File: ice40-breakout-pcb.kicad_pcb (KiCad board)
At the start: 2 copper layers, 56 x 78.3 mm, 59 parts, among them J1 USB_B_Micro, J2 USB_Break_Out, J3 Conn_02x16_Odd_Even, J4 Conn_02x16_Odd_Even, J5 Conn_02x16_Odd_Even, J6 Conn_02x04_Odd_Even, U1 SIT2001BI-S2-33E-12.000000G, U2 TLV73333PDBV, U3 TLV73312PDBV, U4 AT25SF081-SHD-X, U5 ICE40HX4K-TQ144

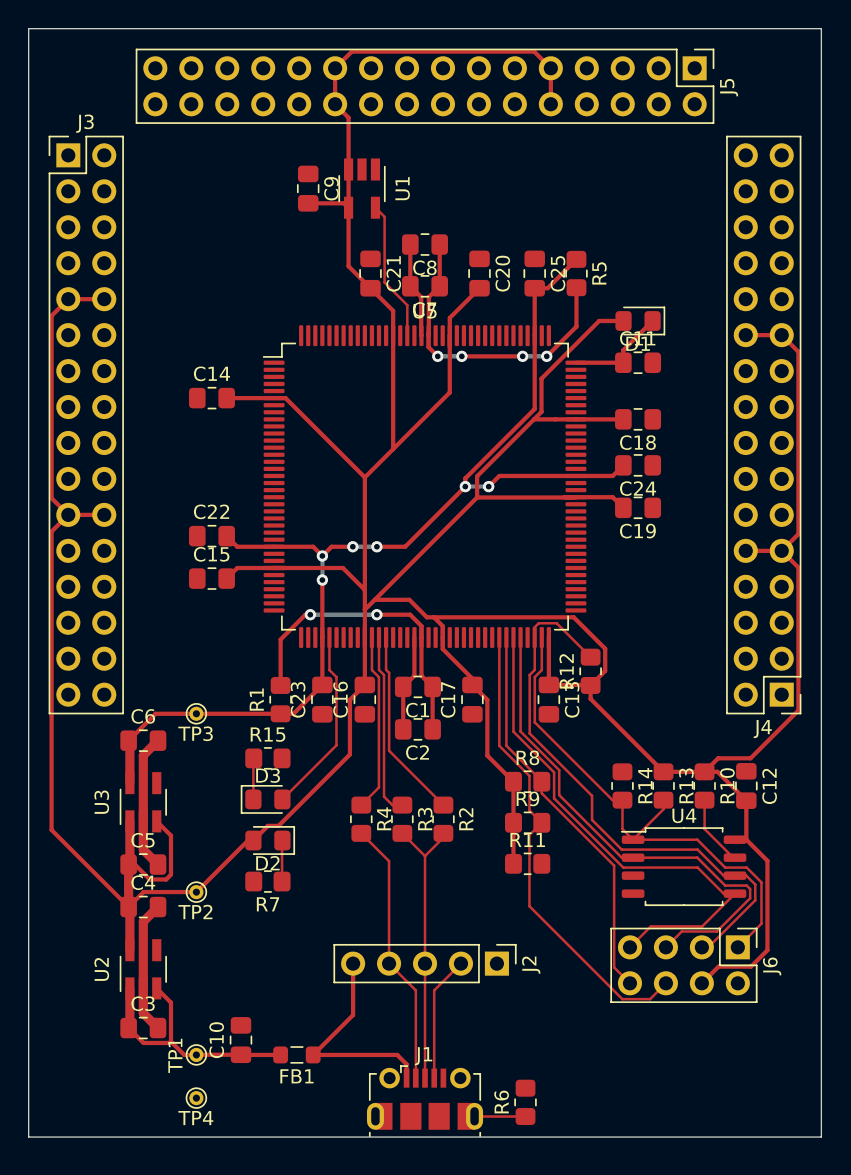
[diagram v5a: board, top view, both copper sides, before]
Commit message: Initial routing of GPIO.
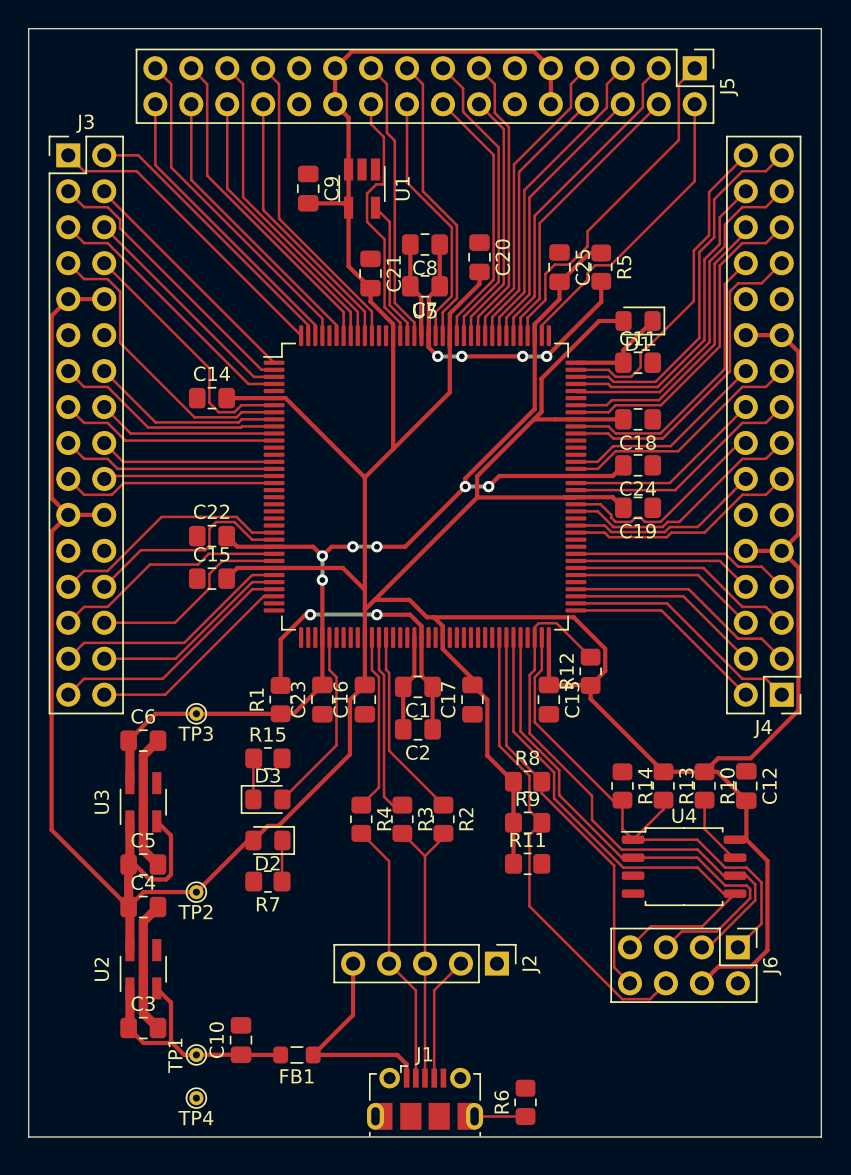
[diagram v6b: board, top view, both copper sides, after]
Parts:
- moved C25 1.81 mm to (129.5, 74.5)
- moved R5 1.81 mm to (132.4, 74.5)
- moved C20 1.15 mm to (123.8, 73.8)
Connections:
- J3 pad 1: Net-(J3-Pad1) -> gp_a_1
- J3 pad 13: Net-(J3-Pad13) -> gp_a_9
- J3 pad 14: Net-(J3-Pad14) -> gp_a_10
- J3 pad 15: Net-(J3-Pad15) -> gp_a_11
- J3 pad 16: Net-(J3-Pad16) -> gp_a_12
- J3 pad 17: Net-(J3-Pad17) -> gp_a_13
- J3 pad 18: Net-(J3-Pad18) -> gp_a_14
- J3 pad 19: Net-(J3-Pad19) -> gp_a_15
- J3 pad 2: Net-(J3-Pad2) -> gp_a_2
- J3 pad 20: Net-(J3-Pad20) -> gp_a_16
- J3 pad 25: Net-(J3-Pad25) -> gp_a_17
- J3 pad 26: Net-(J3-Pad26) -> gp_a_18
- J3 pad 27: Net-(J3-Pad27) -> gp_a_19
- J3 pad 28: Net-(J3-Pad28) -> gp_a_20
- J3 pad 29: Net-(J3-Pad29) -> gp_a_21
- J3 pad 3: Net-(J3-Pad3) -> gp_a_3
- J3 pad 30: Net-(J3-Pad30) -> gp_a_22
- J3 pad 31: Net-(J3-Pad31) -> gp_a_23
- J3 pad 32: Net-(J3-Pad32) -> gp_a_24
- J3 pad 4: Net-(J3-Pad4) -> gp_a_4
- J3 pad 5: Net-(J3-Pad5) -> gp_a_5
- J3 pad 6: Net-(J3-Pad6) -> gp_a_6
- J3 pad 7: Net-(J3-Pad7) -> gp_a_7
- J3 pad 8: Net-(J3-Pad8) -> gp_a_8
- J4 pad 1: Net-(J4-Pad1) -> gp_c_1
- J4 pad 13: Net-(J4-Pad13) -> gp_c_9
- J4 pad 14: Net-(J4-Pad14) -> gp_c_10
- J4 pad 15: Net-(J4-Pad15) -> gp_c_11
- J4 pad 16: Net-(J4-Pad16) -> gp_c_12
- J4 pad 17: Net-(J4-Pad17) -> gp_c_13
- J4 pad 18: Net-(J4-Pad18) -> gp_c_14
- J4 pad 19: Net-(J4-Pad19) -> gp_c_15
- J4 pad 2: Net-(J4-Pad2) -> gp_c_2
- J4 pad 20: Net-(J4-Pad20) -> gp_c_16
- J4 pad 25: Net-(J4-Pad25) -> gp_c_17
- J4 pad 26: Net-(J4-Pad26) -> gp_c_18
- J4 pad 27: Net-(J4-Pad27) -> gp_c_19
- J4 pad 28: Net-(J4-Pad28) -> gp_c_20
- J4 pad 29: Net-(J4-Pad29) -> gp_c_21
- J4 pad 3: Net-(J4-Pad3) -> gp_c_3
- J4 pad 30: Net-(J4-Pad30) -> gp_c_22
- J4 pad 31: Net-(J4-Pad31) -> gp_c_23
- J4 pad 32: Net-(J4-Pad32) -> gp_c_24
- J4 pad 4: Net-(J4-Pad4) -> gp_c_4
- J4 pad 5: Net-(J4-Pad5) -> gp_c_5
- J4 pad 6: Net-(J4-Pad6) -> gp_c_6
- J4 pad 7: Net-(J4-Pad7) -> gp_c_7
- J4 pad 8: Net-(J4-Pad8) -> gp_c_8
- J5 pad 1: Net-(J5-Pad1) -> gp_b_1
- J5 pad 13: Net-(J5-Pad13) -> gp_b_9
- J5 pad 14: Net-(J5-Pad14) -> gp_b_10
- J5 pad 15: Net-(J5-Pad15) -> gp_b_11
- J5 pad 16: Net-(J5-Pad16) -> gp_b_12
- J5 pad 17: Net-(J5-Pad17) -> gp_b_13
- J5 pad 18: Net-(J5-Pad18) -> gp_b_14
- J5 pad 19: Net-(J5-Pad19) -> gp_b_15
- J5 pad 2: Net-(J5-Pad2) -> gp_b_2
- J5 pad 20: Net-(J5-Pad20) -> gp_b_16
- J5 pad 25: Net-(J5-Pad25) -> gp_b_17
- J5 pad 26: Net-(J5-Pad26) -> gp_b_18
- J5 pad 27: Net-(J5-Pad27) -> gp_b_19
- J5 pad 28: Net-(J5-Pad28) -> gp_b_20
- J5 pad 29: Net-(J5-Pad29) -> gp_b_21
- J5 pad 3: Net-(J5-Pad3) -> gp_b_3
- J5 pad 30: Net-(J5-Pad30) -> gp_b_22
- J5 pad 31: Net-(J5-Pad31) -> gp_b_23
- J5 pad 32: Net-(J5-Pad32) -> gp_b_24
- J5 pad 4: Net-(J5-Pad4) -> gp_b_4
- J5 pad 5: Net-(J5-Pad5) -> gp_b_5
- J5 pad 6: Net-(J5-Pad6) -> gp_b_6
- J5 pad 7: Net-(J5-Pad7) -> gp_b_7
- J5 pad 8: Net-(J5-Pad8) -> gp_b_8
- U5 pad 1: Net-(U5-Pad1) -> gp_a_4
- U5 pad 10: Net-(U5-Pad10) -> gp_a_9
- U5 pad 101: Net-(U5-Pad101) -> gp_c_19
- U5 pad 102: Net-(U5-Pad102) -> gp_c_20
- U5 pad 104: Net-(U5-Pad104) -> gp_c_21
- U5 pad 105: Net-(U5-Pad105) -> gp_c_22
- U5 pad 106: Net-(U5-Pad106) -> gp_c_23
- U5 pad 107: Net-(U5-Pad107) -> gp_c_24
- U5 pad 11: Net-(U5-Pad11) -> gp_a_12
- U5 pad 110: Net-(U5-Pad110) -> gp_b_2
- U5 pad 112: Net-(U5-Pad112) -> gp_b_1
- U5 pad 113: Net-(U5-Pad113) -> gp_b_4
- U5 pad 114: Net-(U5-Pad114) -> gp_b_3
- U5 pad 115: Net-(U5-Pad115) -> gp_b_6
- U5 pad 116: Net-(U5-Pad116) -> gp_b_5
- U5 pad 117: Net-(U5-Pad117) -> gp_b_8
- U5 pad 118: Net-(U5-Pad118) -> gp_b_7
- U5 pad 119: Net-(U5-Pad119) -> gp_b_9
- U5 pad 12: Net-(U5-Pad12) -> gp_a_11
- U5 pad 120: Net-(U5-Pad120) -> gp_b_10
- U5 pad 121: Net-(U5-Pad121) -> gp_b_11
- U5 pad 122: Net-(U5-Pad122) -> gp_b_12
- U5 pad 124: Net-(U5-Pad124) -> gp_b_13
- U5 pad 125: Net-(U5-Pad125) -> gp_b_14
- U5 pad 128: Net-(U5-Pad128) -> gp_b_15
- U5 pad 130: Net-(U5-Pad130) -> gp_b_16
- U5 pad 134: Net-(U5-Pad134) -> gp_b_17
- U5 pad 135: Net-(U5-Pad135) -> gp_b_18
- U5 pad 136: Net-(U5-Pad136) -> gp_b_19
- U5 pad 137: Net-(U5-Pad137) -> gp_b_20
- U5 pad 138: Net-(U5-Pad138) -> gp_b_21
- U5 pad 139: Net-(U5-Pad139) -> gp_b_22
- U5 pad 141: Net-(U5-Pad141) -> gp_b_23
- U5 pad 142: Net-(U5-Pad142) -> gp_b_24
- U5 pad 143: Net-(U5-Pad143) -> gp_a_2
- U5 pad 144: Net-(U5-Pad144) -> gp_a_1
- U5 pad 15: Net-(U5-Pad15) -> gp_a_14
- U5 pad 16: Net-(U5-Pad16) -> gp_a_13
- U5 pad 17: Net-(U5-Pad17) -> gp_a_16
- U5 pad 18: Net-(U5-Pad18) -> gp_a_15
- U5 pad 2: Net-(U5-Pad2) -> gp_a_3
- U5 pad 25: Net-(U5-Pad25) -> gp_a_17
- U5 pad 26: Net-(U5-Pad26) -> gp_a_18
- U5 pad 28: Net-(U5-Pad28) -> gp_a_19
- U5 pad 29: Net-(U5-Pad29) -> gp_a_20
- U5 pad 3: Net-(U5-Pad3) -> gp_a_6
- U5 pad 31: Net-(U5-Pad31) -> gp_a_21
- U5 pad 32: Net-(U5-Pad32) -> gp_a_22
- U5 pad 33: Net-(U5-Pad33) -> gp_a_23
- U5 pad 34: Net-(U5-Pad34) -> gp_a_24
- U5 pad 4: Net-(U5-Pad4) -> gp_a_5
- U5 pad 7: Net-(U5-Pad7) -> gp_a_8
- U5 pad 73: Net-(U5-Pad73) -> gp_c_2
- U5 pad 74: Net-(U5-Pad74) -> gp_c_1
- U5 pad 75: Net-(U5-Pad75) -> gp_c_4
- U5 pad 76: Net-(U5-Pad76) -> gp_c_3
- U5 pad 78: Net-(U5-Pad78) -> gp_c_6
- U5 pad 79: Net-(U5-Pad79) -> gp_c_5
- U5 pad 8: Net-(U5-Pad8) -> gp_a_7
- U5 pad 80: Net-(U5-Pad80) -> gp_c_8
- U5 pad 81: Net-(U5-Pad81) -> gp_c_7
- U5 pad 84: Net-(U5-Pad84) -> gp_c_9
- U5 pad 85: Net-(U5-Pad85) -> gp_c_10
- U5 pad 87: Net-(U5-Pad87) -> gp_c_11
- U5 pad 88: Net-(U5-Pad88) -> gp_c_12
- U5 pad 9: Net-(U5-Pad9) -> gp_a_10
- U5 pad 90: Net-(U5-Pad90) -> gp_c_13
- U5 pad 91: Net-(U5-Pad91) -> gp_c_14
- U5 pad 93: Net-(U5-Pad93) -> gp_c_15
- U5 pad 94: Net-(U5-Pad94) -> gp_c_16
- U5 pad 98: Net-(U5-Pad98) -> gp_c_17
- U5 pad 99: Net-(U5-Pad99) -> gp_c_18
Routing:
- net gp_c_23: track 0.00 -> 26.4 mm
- net gp_c_21: track 0.00 -> 24.7 mm
- net gp_b_1: track 0.00 -> 24.4 mm
- net gp_b_23: track 0.00 -> 23.8 mm
- net gp_b_21: track 0.00 -> 23.3 mm
- net gp_c_19: track 0.00 -> 23.3 mm
- net gp_c_24: track 0.00 -> 23.2 mm
- net gp_b_3: track 0.00 -> 23.1 mm
- net gp_c_17: track 0.00 -> 23.1 mm
- net gp_b_19: track 0.00 -> 22.7 mm
- net gp_b_5: track 0.00 -> 22.5 mm
- net gp_c_22: track 0.00 -> 22.3 mm
- net gp_b_17: track 0.00 -> 22.1 mm
- net gp_b_7: track 0.00 -> 21.9 mm
- net gp_a_1: track 0.00 -> 21.7 mm
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
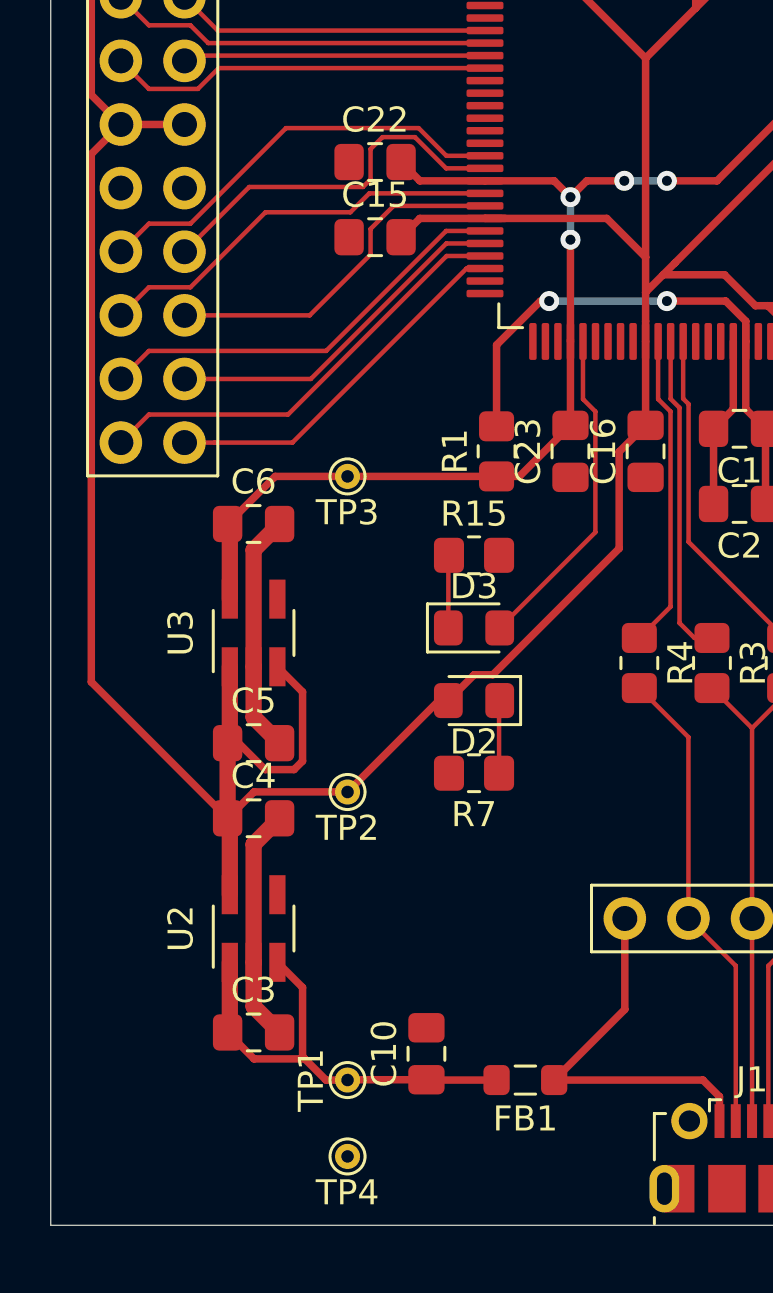
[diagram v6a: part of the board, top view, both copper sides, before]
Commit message: Reposition voltage regulators for more compact layout.
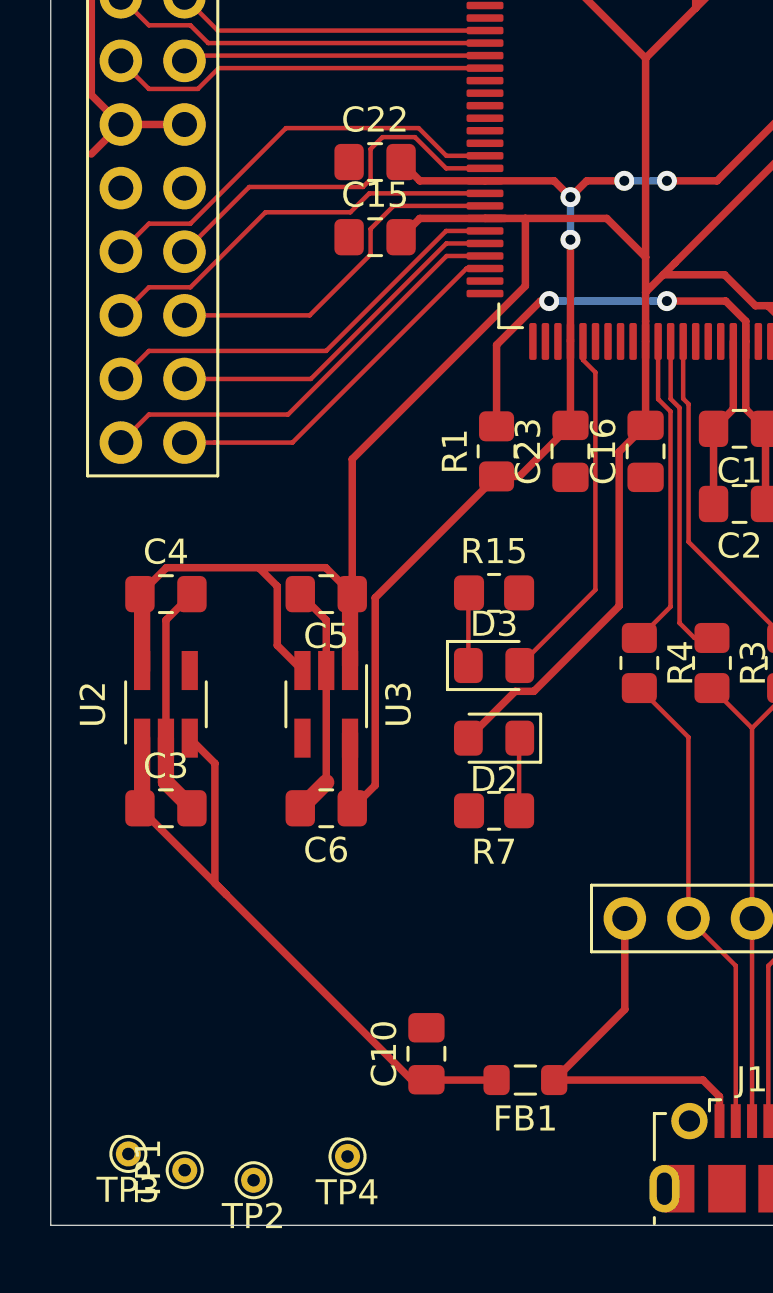
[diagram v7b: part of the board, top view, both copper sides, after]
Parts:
- moved TP3 28.4 mm to (95.1, 133.1)
- moved TP2 15.9 mm to (100.1, 134.2)
- moved C6 11.7 mm to (103.0, 119.3), turned to 180 degrees
- moved C3 9.61 mm to (96.6, 119.3)
- moved C4 9.61 mm to (96.6, 110.8)
- moved U2 9.61 mm to (96.6, 115.2)
- moved TP1 7.43 mm to (97.3, 133.8)
- moved C5 6.62 mm to (103.0, 110.8), turned to 180 degrees
- moved U3 4.07 mm to (103.0, 115.2), turned to 270 degrees
- moved D2 1.70 mm to (109.7, 116.5)
- moved D3 1.70 mm to (109.7, 113.6)
- moved R15 1.70 mm to (109.7, 110.7)
- moved R7 1.70 mm to (109.7, 119.4)
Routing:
- net +3V3: track 369.0 -> 351.7 mm
- net +5V: track 18.7 -> 28.4 mm
- net +1V2: track 79.9 -> 84.0 mm
- net LED: track 13.2 -> 14.4 mm

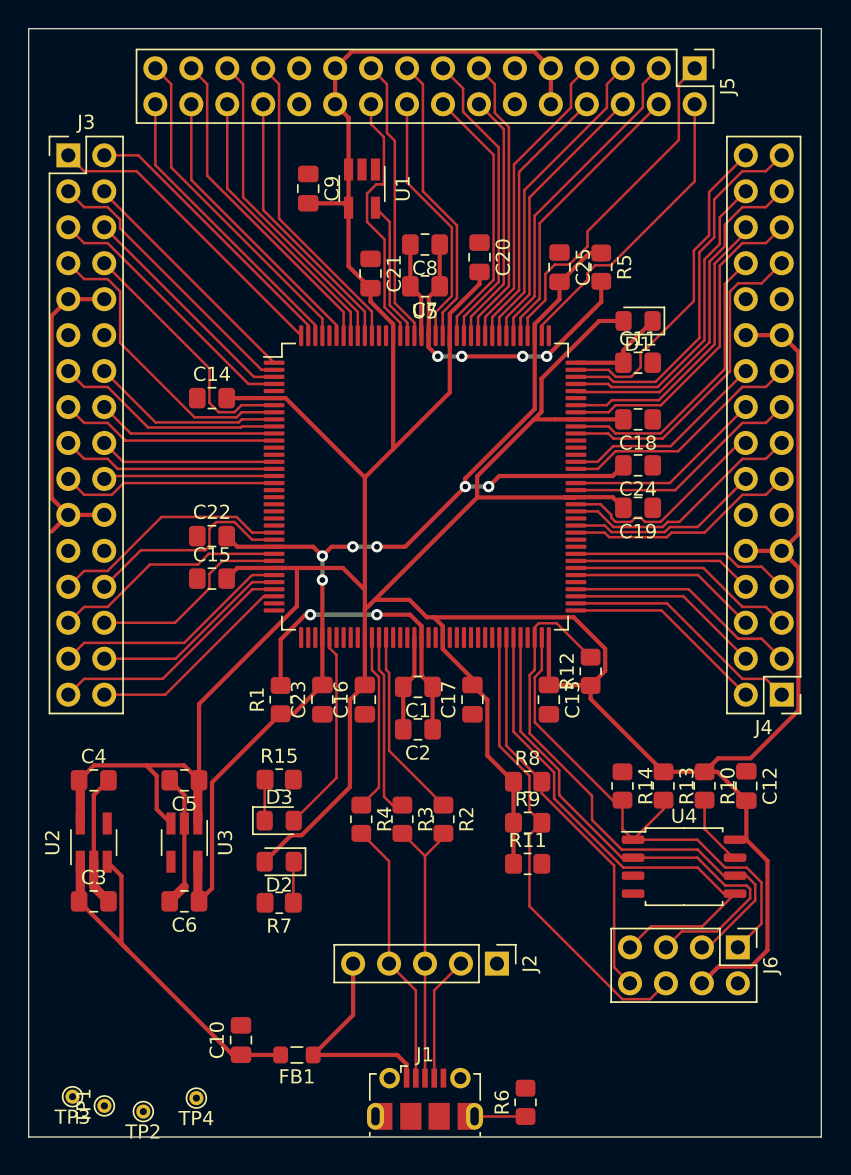
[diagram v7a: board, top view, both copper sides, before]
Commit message: Shorten the board.
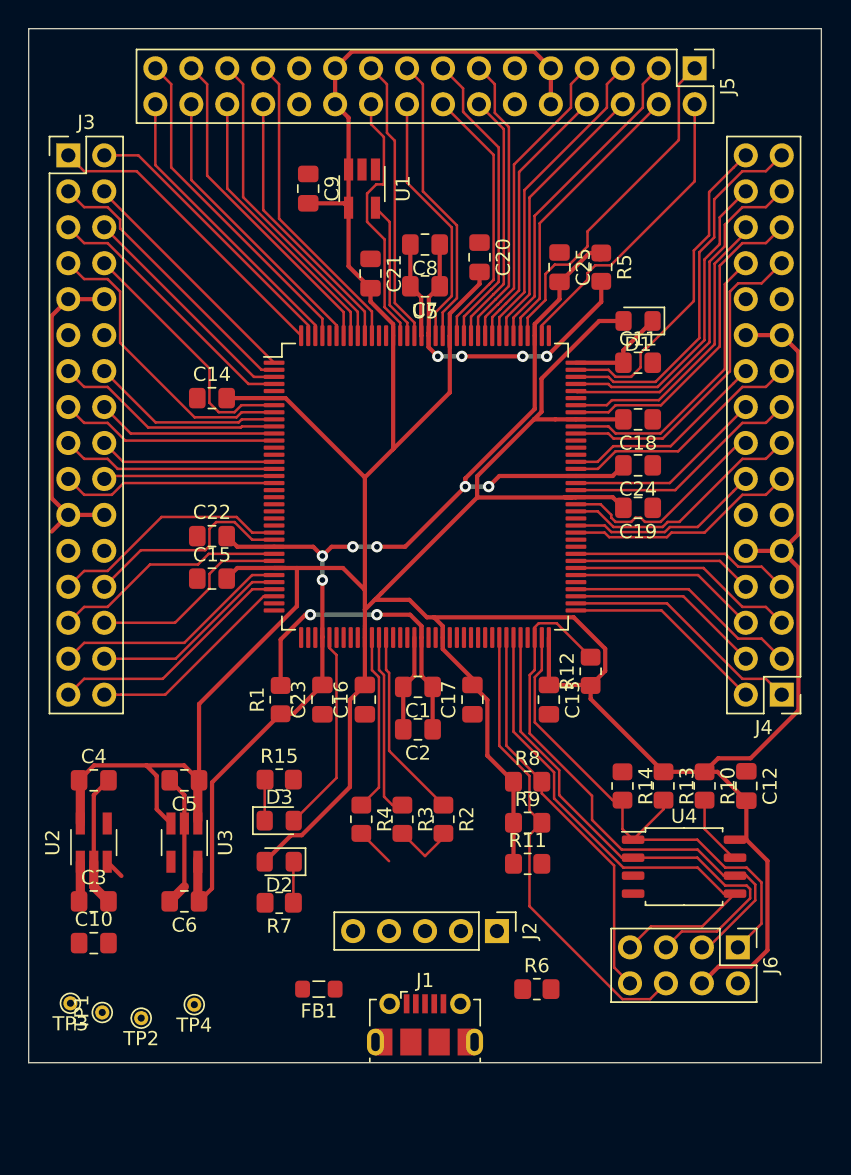
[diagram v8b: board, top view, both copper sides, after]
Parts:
- moved C10 12.5 mm to (96.6, 122.2), turned to 0 degrees
- moved R6 8.04 mm to (127.9, 125.5), turned to 0 degrees
- moved TP2 6.60 mm to (100.0, 127.5)
- moved TP1 6.60 mm to (97.2, 127.2)
- moved TP3 6.60 mm to (95.0, 126.5)
- moved TP4 6.60 mm to (103.7, 126.6)
- moved J1 5.25 mm to (120.0, 128.0)
- moved FB1 4.90 mm to (112.5, 125.5)
- moved J2 2.30 mm to (125.1, 121.4)
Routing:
- net +5V: track 28.4 -> 4.26 mm
- net Net-(J1-Pad2): track 18.9 -> 2.77 mm
- net Net-(J1-Pad3): track 20.1 -> 4.40 mm
- net Net-(FB1-Pad1): track 15.5 -> 0.00 mm
- net Net-(J1-Pad4): track 8.87 -> 0.00 mm
- net Net-(J1-Pad6): track 3.61 -> 0.00 mm
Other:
- board size 56 x 78.3 mm -> 56 x 73 mm
